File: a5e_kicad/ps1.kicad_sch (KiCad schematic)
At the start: 80 parts, among them U16 AP61202Z6, U18 AP61202Z6, U19 AP61202Z6, U8 AP61202Z6

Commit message: Add LCSC part numbers and fix C102 footprint
Add a hidden LCSC field to 290 symbols from the JLCPCB parts match
(2026-10-23). Left without LCSC: U7, U15, L1 (not in the JLCPCB
library), C1/C2/C4 and L2-L5 (no value specified), J3 (no confident
match) and Y3 (the 12 pF Basic crystal does not suit the 27 pF load
caps). U2, U12, Y2 and J9 carry the exact-MPN LCSC numbers although
they currently show zero JLCPCB stock.

C102 (22U 6V3) had a 0201 footprint; no 22 uF 0201 part exists. Change
it to 0402 (C415703) like C5-C7.
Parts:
- C116, C117, C118, C119: LCSC (none) -> C1562
- C157, C158, C159, C160, C161, C163, C164, C165, C167, C169, C170, C171, C172, C173, C196, C203, C204, C205, C216, C217: LCSC (none) -> C415703
- C162: LCSC (none) -> C1525
- C174, C175, C176, C177, C178, C179, C180, C181, C182, C183, C184, C185, C186, C187, C189, C190, C191, C192, C193, C194, C195, C197, C206, C207, C208, C209, C210, C214, C215, C218, C219, C220, C221: LCSC (none) -> C190183
- R249, R80, R81, R82, R85, R86, R88, R91: LCSC (none) -> C25744
- R65: LCSC (none) -> C25792
- R83: LCSC (none) -> C25879
- R89: LCSC (none) -> C25752
- U16, U18, U19, U8: LCSC (none) -> C5188956

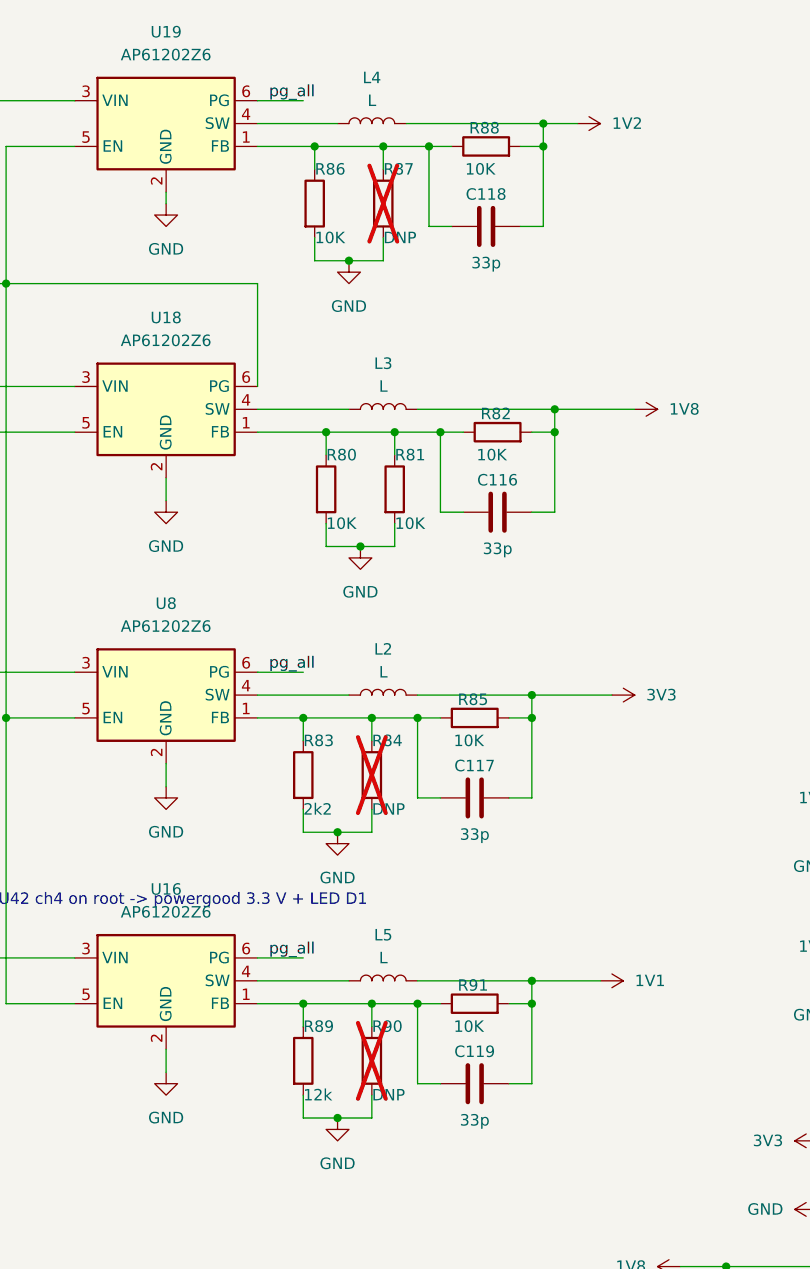
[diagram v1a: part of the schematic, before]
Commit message: U9 to LVDS AX3DAF1, AP61202 dividers to data sheet values
- U9 AX3HAF1 (HCSL) -> AX3DAF1-100.0000T (LVDS, C2002827), same AX3
  pinout. The HCSL part needs 50R to GND at its outputs, which the board
  doesn't have (R27/R28 are behind the AC-coupling caps, to VICM). LVDS
  works with the existing AC coupling, 2x50R termination and bias.
- AP61202 feedback dividers use the data sheet table 1 values with 200k
  top, so the 33 pF feed-forward caps (C116-C119) sit where intended:
  1V8 200k/100k (R81 DNP), 3V3 200k/44.2k, 1V2 200k/200k, 1V1 200k/240k.
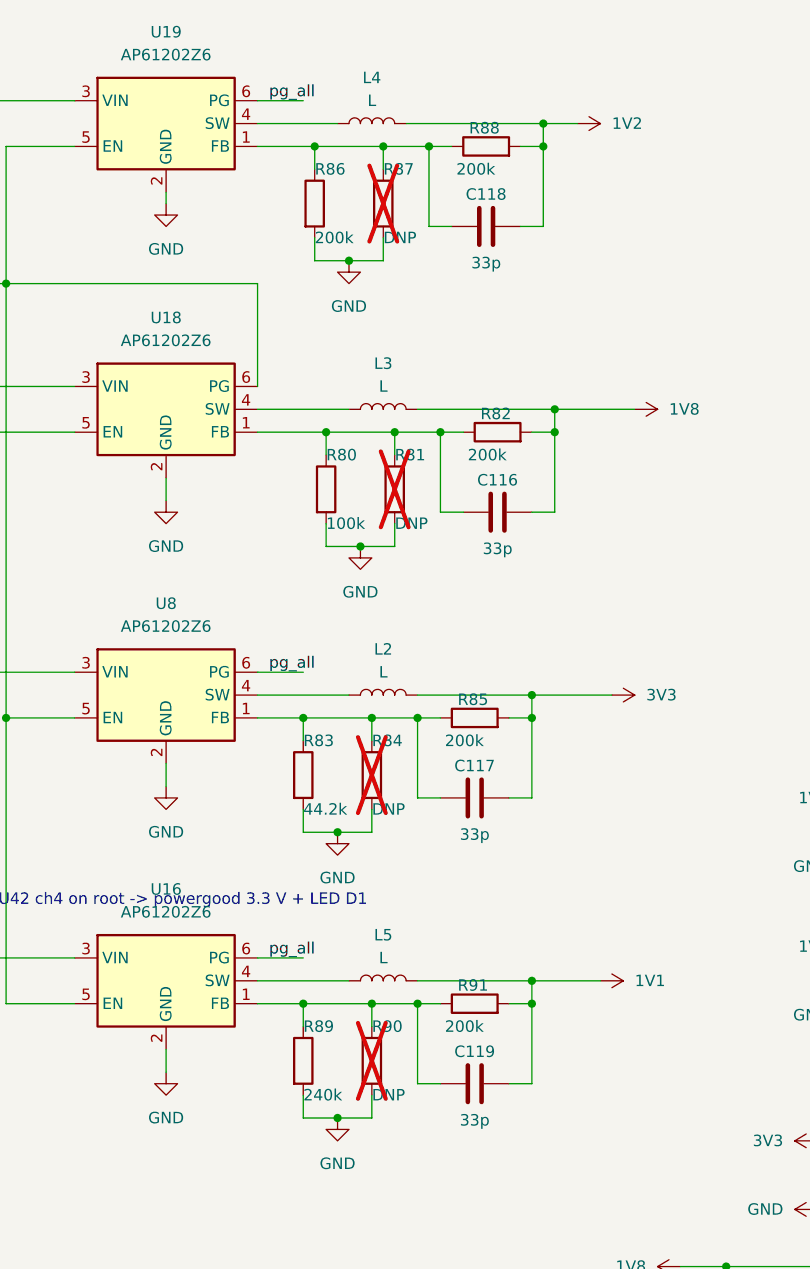
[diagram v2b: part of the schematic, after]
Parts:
- R80: value 10K -> 100k; LCSC C25744 -> C25741
- R81: value 10K -> DNP; LCSC C25744 -> (none); now not fitted
- R82, R85, R86, R88, R91: value 10K -> 200k; LCSC C25744 -> C25764
- R83: value 2k2 -> 44.2k; LCSC C25879 -> C25895
- R89: value 12k -> 240k; LCSC C25752 -> C64043
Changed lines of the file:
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@@
 			)
 		)
-		(property "Value" "10K"
+		(property "Value" "200k"
 			(at 129.286 31.75 90)
 			(show_name no)
@@
 			)
 		)
-		(property "LCSC" "C25744"
+		(property "LCSC" "C25764"
 			(at 128.27 30.988 90)
 			(hide yes)
@@
 			)
 		)
-		(property "Value" "10K"
+		(property "Value" "200k"
 			(at 128.016 95.25 90)
 			(show_name no)
@@
 			)
 		)
-		(property "LCSC" "C25744"
+		(property "LCSC" "C25764"
 			(at 127 94.488 90)
 			(hide yes)
@@
 		(on_board yes)
 		(in_pos_files yes)
-		(dnp no)
+		(dnp yes)
 		(property "Reference" "R81"
 			(at 118.11 63.5 0)
@@
 			)
 		)
-		(property "Value" "10K"
+		(property "Value" "DNP"
 			(at 118.11 71.12 0)
 			(show_name no)
@@
 			)
 		)
-		(property "LCSC" "C25744"
+		(property "LCSC" ""
 			(at 116.332 67.31 90)
 			(hide yes)
@@
 			)
 		)
-		(property "Value" "10K"
+		(property "Value" "200k"
 			(at 130.556 63.5 90)
 			(show_name no)
@@
 			)
 		)
-		(property "LCSC" "C25744"
+		(property "LCSC" "C25764"
 			(at 129.54 62.738 90)
 			(hide yes)
@@
 			)
 		)
-		(property "Value" "10K"
+		(property "Value" "200k"
 			(at 128.016 127 90)
 			(show_name no)
@@
 			)
 		)
-		(property "LCSC" "C25744"
+		(property "LCSC" "C25764"
 			(at 127 126.238 90)
 			(hide yes)
@@
 			)
 		)
-		(property "Value" "2k2"
+		(property "Value" "44.2k"
 			(at 107.95 102.87 0)
 			(show_name no)
@@
 			)
 		)
-		(property "LCSC" "C25879"
+		(property "LCSC" "C25895"
 			(at 106.172 99.06 90)
 			(hide yes)
@@
 			)
 		)
-		(property "Value" "12k"
+		(property "Value" "240k"
 			(at 107.95 134.62 0)
 			(show_name no)
@@
 			)
 		)
-		(property "LCSC" "C25752"
+		(property "LCSC" "C64043"
 			(at 106.172 130.81 90)
 			(hide yes)
@@
 			)
 		)
-		(property "Value" "10K"
+		(property "Value" "200k"
 			(at 109.22 39.37 0)
 			(show_name no)
@@
 			)
 		)
-		(property "LCSC" "C25744"
+		(property "LCSC" "C25764"
 			(at 107.442 35.56 90)
 			(hide yes)
@@
 			)
 		)
-		(property "Value" "10K"
+		(property "Value" "100k"
 			(at 110.49 71.12 0)
 			(show_name no)
@@
 			)
 		)
-		(property "LCSC" "C25744"
+		(property "LCSC" "C25741"
 			(at 108.712 67.31 90)
 			(hide yes)

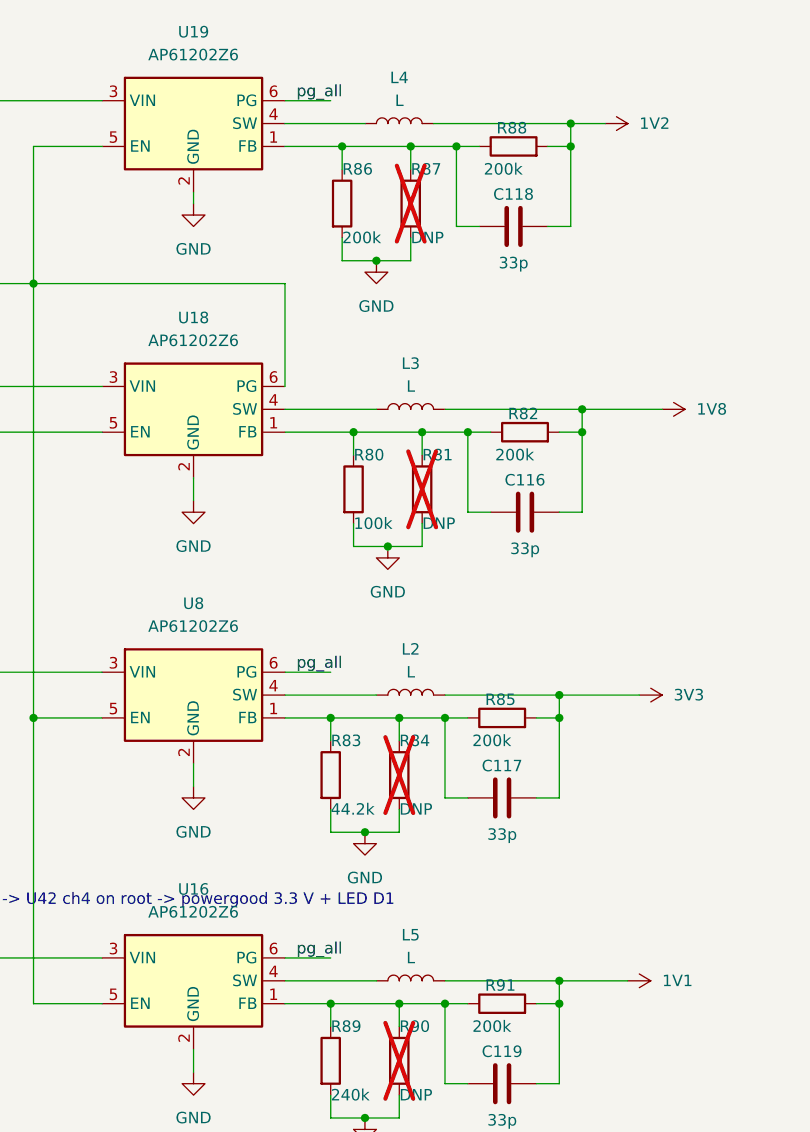
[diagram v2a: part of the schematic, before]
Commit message: L2-L5 1uH (as on the Agilex 3 card), Quartus EMIF/power results recorded
- L2-L5 (3V3/1V8/1V2/1V1 AP61202 bucks) = 1 uH Cenker CKCS201610,
  C97002, the same as on the Agilex 3 card. The AP61202 data sheet asks
  for 1.0-1.5 uH. Per-rail loads from Quartus are 0.2-0.45 A plus board
  loads. The footprint changes from 0805 to 2016.
- Bank 3 note: LPDDR4 1600 MT/s with a 100 MHz U9 refclk, tested in
  Quartus (was the stale 111.111 MHz).
- LPDDR4_SWIZZLE_PLAN.md: both pinout variants pass the fitter;
  swizzle strings, negative control, refclk and refresh-timing notes.
- Checklist: per-rail FPGA power from the Quartus Power Analyzer.
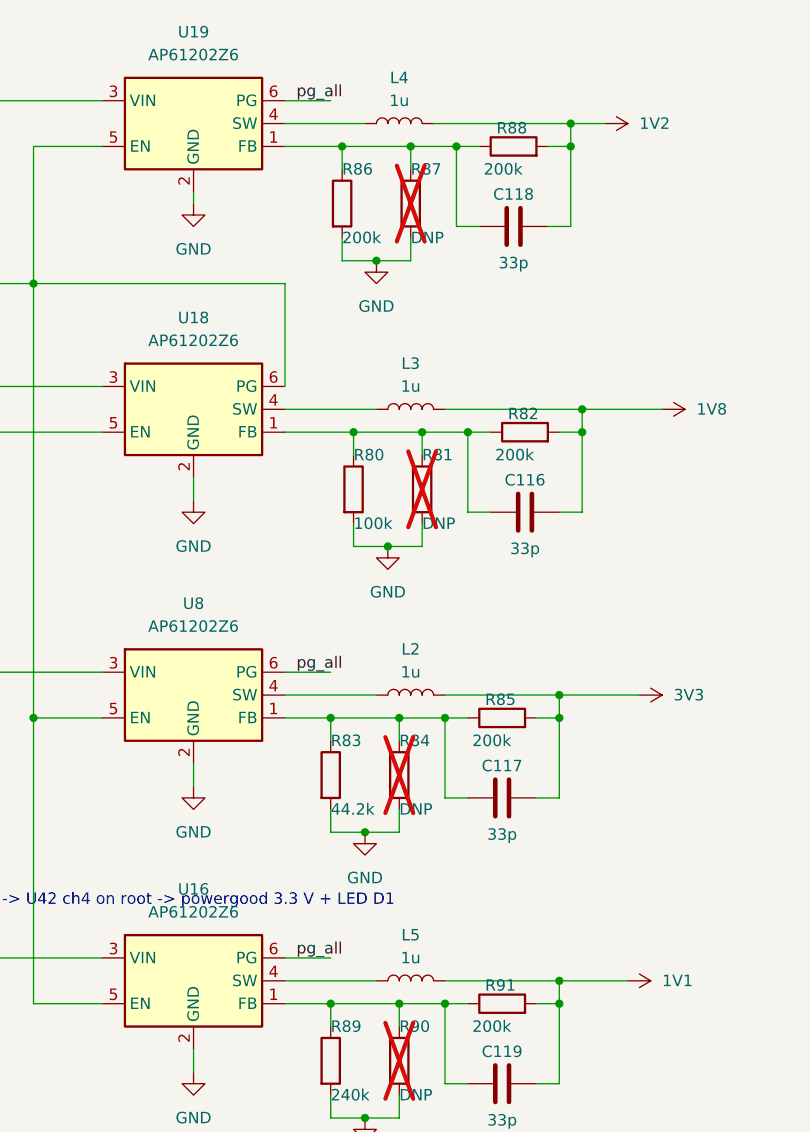
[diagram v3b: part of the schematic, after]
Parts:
- L2, L3, L4, L5: value L -> 1u; footprint Inductor_SMD:L_0805_2012Metric -> Inductor_SMD:L_Cenker_CKCS201610; LCSC (none) -> C97002
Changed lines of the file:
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@@
 			)
 		)
-		(property "Value" "L"
+		(property "Value" "1u"
 			(at 116.84 55.88 90)
 			(show_name no)
@@
 			)
 		)
-		(property "Footprint" "Inductor_SMD:L_0805_2012Metric"
+		(property "LCSC" "C97002"
+			(at 116.84 58.42 0)
+			(hide yes)
+			(show_name no)
+			(do_not_autoplace no)
+			(effects
+				(font
+					(size 1.27 1.27)
+				)
+			)
+		)
+		(property "Footprint" "Inductor_SMD:L_Cenker_CKCS201610"
 			(at 116.84 58.42 0)
 			(hide yes)
@@
 			)
 		)
-		(property "Value" "L"
+		(property "Value" "1u"
 			(at 115.57 24.13 90)
 			(show_name no)
@@
 			)
 		)
-		(property "Footprint" "Inductor_SMD:L_0805_2012Metric"
+		(property "LCSC" "C97002"
+			(at 115.57 26.67 0)
+			(hide yes)
+			(show_name no)
+			(do_not_autoplace no)
+			(effects
+				(font
+					(size 1.27 1.27)
+				)
+			)
+		)
+		(property "Footprint" "Inductor_SMD:L_Cenker_CKCS201610"
 			(at 115.57 26.67 0)
 			(hide yes)
@@
 			)
 		)
-		(property "Value" "L"
+		(property "Value" "1u"
 			(at 116.84 87.63 90)
 			(show_name no)
@@
 			)
 		)
-		(property "Footprint" "Inductor_SMD:L_0805_2012Metric"
+		(property "LCSC" "C97002"
+			(at 116.84 90.17 0)
+			(hide yes)
+			(show_name no)
+			(do_not_autoplace no)
+			(effects
+				(font
+					(size 1.27 1.27)
+				)
+			)
+		)
+		(property "Footprint" "Inductor_SMD:L_Cenker_CKCS201610"
 			(at 116.84 90.17 0)
 			(hide yes)
@@
 			)
 		)
-		(property "Value" "L"
+		(property "Value" "1u"
 			(at 116.84 119.38 90)
 			(show_name no)
@@
 			)
 		)
-		(property "Footprint" "Inductor_SMD:L_0805_2012Metric"
+		(property "LCSC" "C97002"
 			(at 116.84 121.92 0)
 			(hide yes)
+			(show_name no)
+			(do_not_autoplace no)
+			(effects
+				(font
+					(size 1.27 1.27)
+				)
+			)
+		)
+		(property "Footprint" "Inductor_SMD:L_Cenker_CKCS201610"
+			(at 116.84 121.92 0)
+			(hide yes)

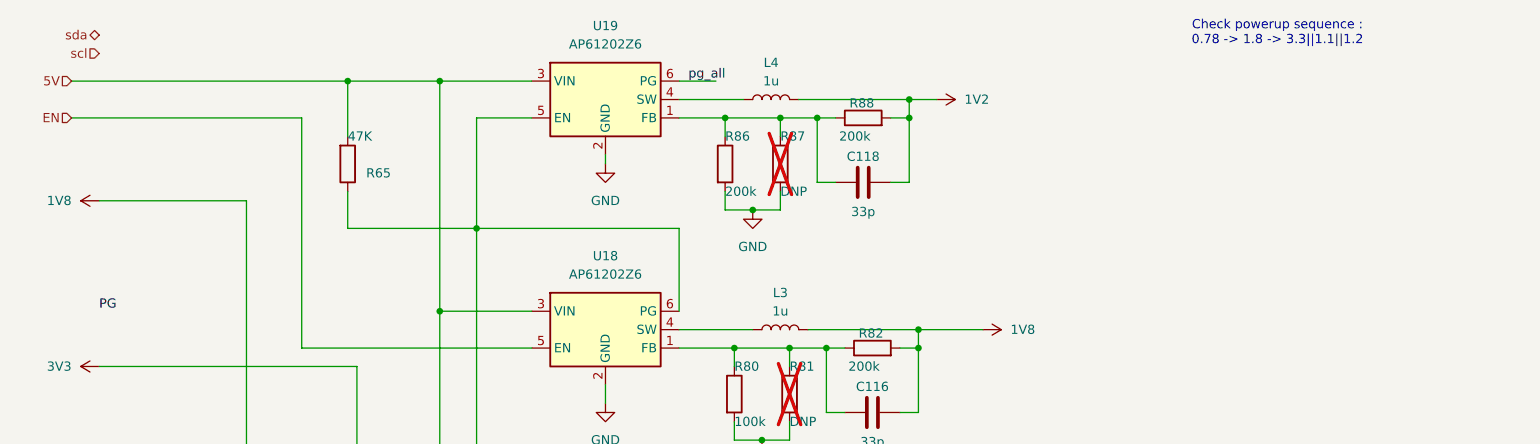
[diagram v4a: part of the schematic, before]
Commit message: Schematic reorg step 1: remove dangling stubs and stale notes, correct notes, fill title blocks
Netlist: 0 renamed, 0 connectivity diffs; DRC parity 0. ERC 315 -> 242.
Plan refreshed for the eMMC, RTL8211FDI, TPS548A28 and the tuned LPDDR4 (IOBANK 3 sheet name kept).
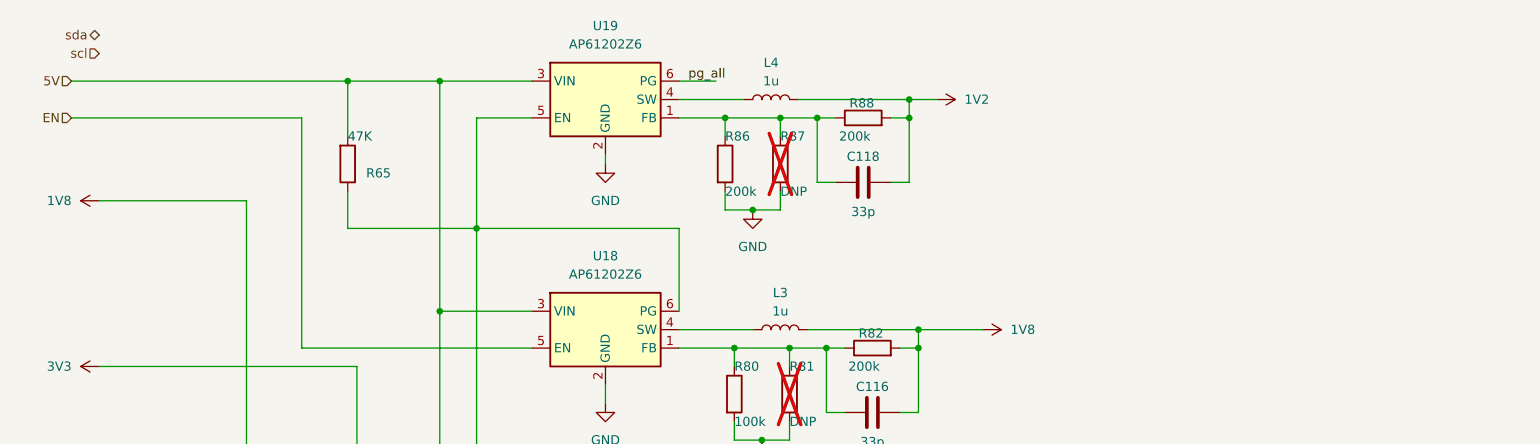
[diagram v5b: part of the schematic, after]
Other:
- note removed: "Check powerup sequence : 0.78 -> 1.8 -> 3.3||1.1||1.2"
- title: (none) -> 1V8 / 3V3 / 1V2 / 1V1 bucks, power good, decoupling
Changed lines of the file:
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@@
 	(paper "A4")
 	(title_block
-		(rev "0.1")
+		(title "1V8 / 3V3 / 1V2 / 1V1 bucks, power good, decoupling")
+		(rev "${REVISION}")
+		(comment 1 "${BOARD}")
 	)
 	(text "PG of 1V2 / 3V3 / 1V1 regulators (open drain) wired-AND, 1.8 V level -> U42 ch4 on root -> powergood 3.3 V + LED D1"
@@
 		)
 	)
-	(text "Check powerup sequence :\n0.78 -> 1.8 -> 3.3||1.1||1.2"
-		(exclude_from_sim no)
-		(at 185.42 17.526 0)
-		(effects
-			(font
-				(size 1.27 1.27)
-			)
-		)
-	)
 	(junction
 		(at 113.03 41.91)
@@
 		)
 	)
-	(label "PG"
-		(at 22.86 55.88 0)
-		(effects
-			(font
-				(size 1.27 1.27)
-			)
-			(justify left bottom)
-		)
-	)
